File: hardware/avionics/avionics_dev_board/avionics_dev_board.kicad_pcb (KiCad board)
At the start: 2 copper layers, 44.6 x 14.1 mm, 13 parts, among them J1 Screw_Term_1x2, SW1 SW_Push, U1 TPS563200

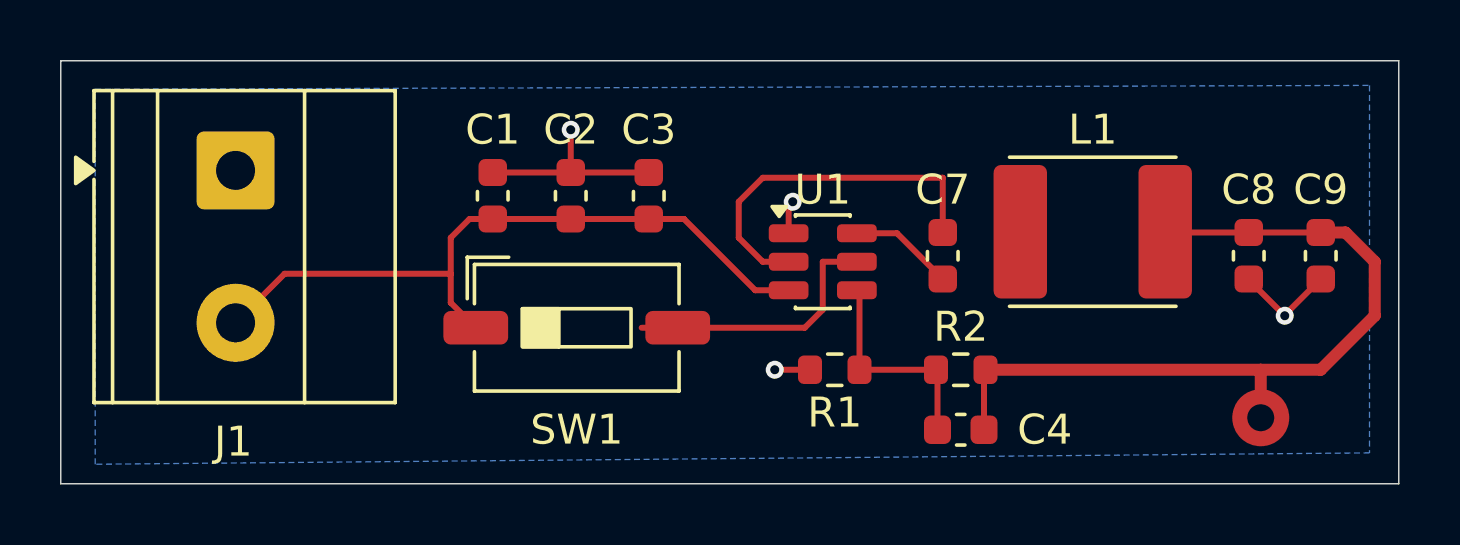
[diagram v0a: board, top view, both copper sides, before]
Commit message: Fixed missing trace on avionics dev pcb
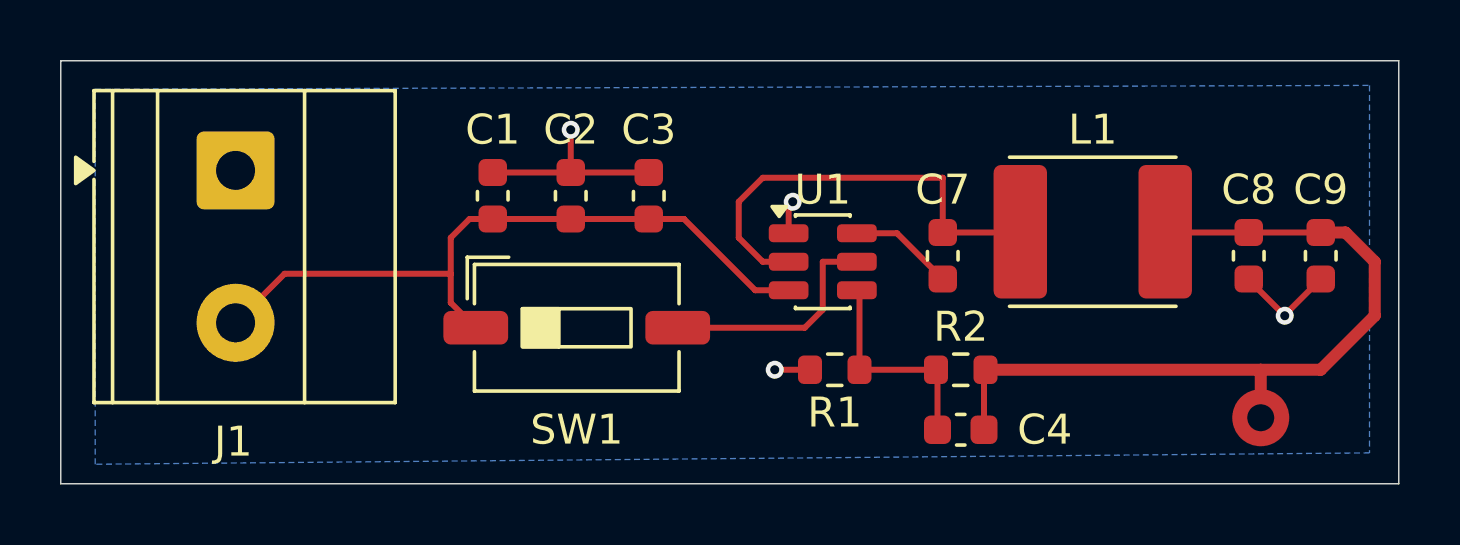
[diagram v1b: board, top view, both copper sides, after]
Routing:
- net Net-(U1-SW): track 12.2 -> 14.7 mm
- net Net-(U1-EN): track 9.02 -> 7.82 mm
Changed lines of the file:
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@@
+	)
+	(segment
+		(start 142.4 109.025)
+		(end 144.96 109.025)
+		(width 0.2)
+		(layer "F.Cu")
+		(net 6)
 	)
 	(segment
@@
 	)
 	(segment
+		(start 144.96 109.025)
+		(end 144.985 109)
+		(width 0.2)
+		(layer "F.Cu")
+		(net 6)
+	)
+	(segment
 		(start 135.6 109.2)
 		(end 135.6 108)
@@
 	)
 	(segment
-		(start 132.365 112.2)
+		(start 133.565 112.2)
 		(end 137.8 112.2)
+		(width 0.2)
+		(layer "F.Cu")
+		(net 7)
+	)
+	(segment
+		(start 137.8 112.2)
+		(end 138.4 111.6)
 		(width 0.2)
 		(layer "F.Cu")
@@
 		(width 0.2)
 		(layer "F.Cu")
-		(net 7)
-	)
-	(segment
-		(start 137.8 112.2)
-		(end 138.4 111.6)
-		(width 0.2)
-		(layer "F.Cu")
